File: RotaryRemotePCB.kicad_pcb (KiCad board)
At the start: 2 copper layers, 82 x 82 mm, 10 parts, among them J1 Conn_01x02, J2 UART, J3 i2c, J4 Neopixel Connector, J5 EncoderRotary, J6 EncoderSwitch, SW1 RotaryEncoder_Switch, U1 TP4056, U2 WeMos_D1_mini

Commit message: Add git submodule
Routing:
- net Net-(U1-Pad6): track 0.00 -> 5.75 mm
- net Net-(U1-Pad5): track 0.00 -> 5.15 mm

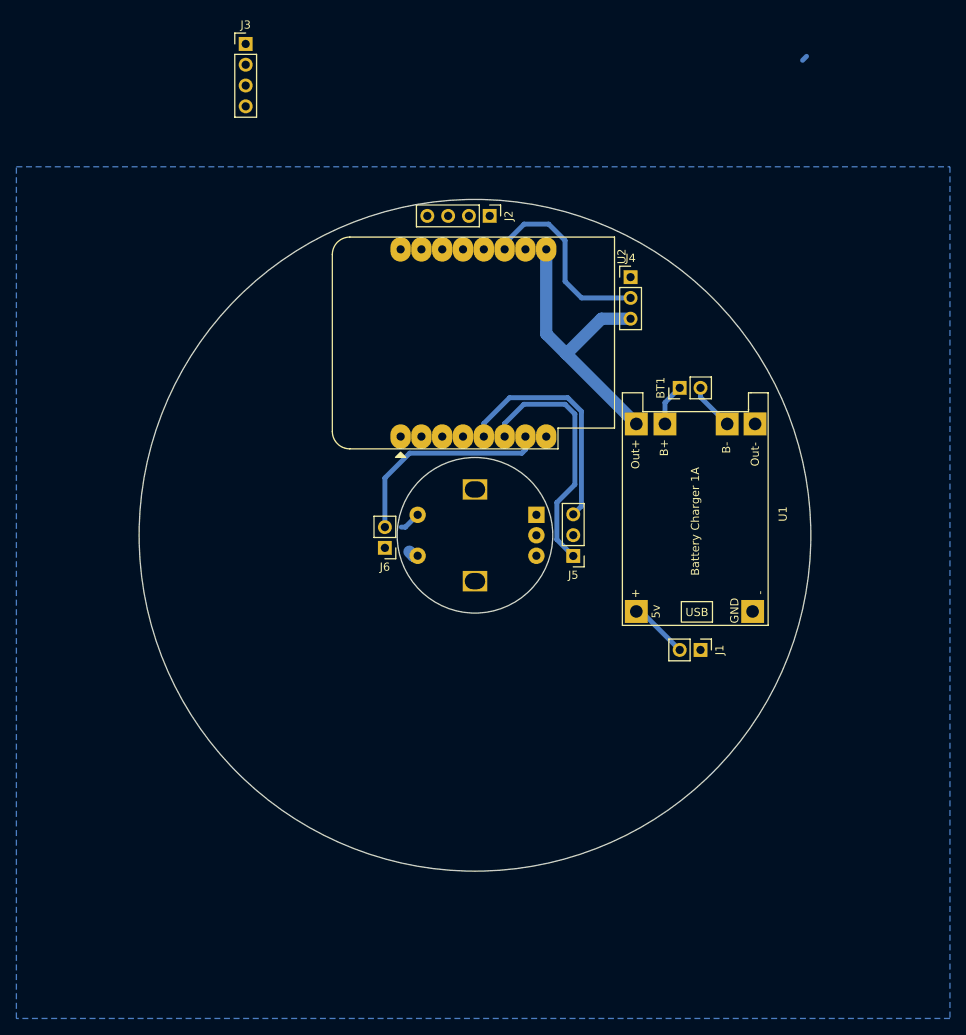
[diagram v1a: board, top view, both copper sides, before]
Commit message: Add FTDI connector
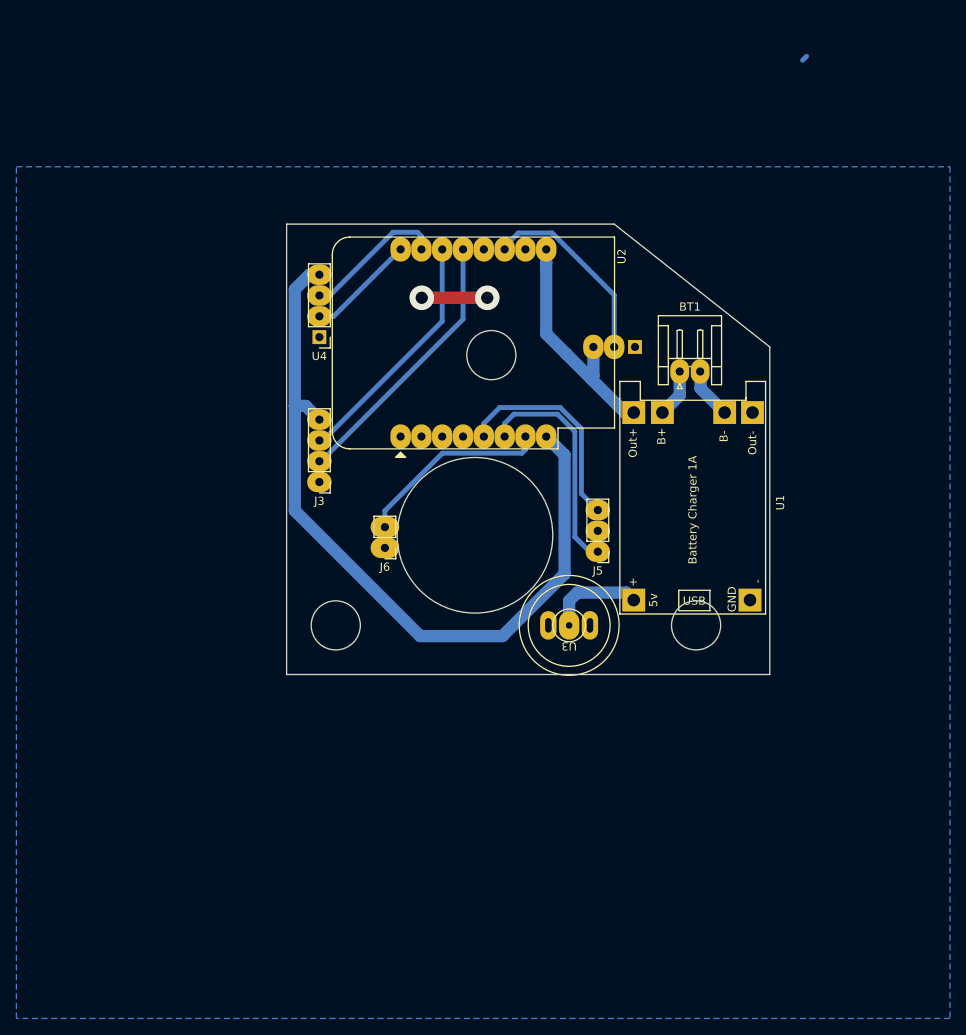
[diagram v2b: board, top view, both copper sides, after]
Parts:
- removed J1: Conn_01x02, Connector_PinHeader_2.54mm:PinHeader_1x02_P2.54mm_Vertical
- removed J2: UART, Connector_PinHeader_2.54mm:PinHeader_1x04_P2.54mm_Vertical
- removed SW1: RotaryEncoder_Switch, Rotary_Encoder:RotaryEncoder_Alps_EC12E-Switch_Vertical_H20mm
- added U3: magnetic-charger, magnetic-charger:magnetic-charger, F.Cu at (111.5, 111.0)
- added U4: TTL, Connector_PinHeader_2.54mm:PinHeader_1x04_P2.54mm_Vertical, F.Cu at (81.0, 75.8)
- BT1: footprint Connector_PinHeader_2.54mm:PinHeader_1x02_P2.54mm_Vertical -> Connector_JST:JST_EH_S2B-EH_1x02_P2.50mm_Horizontal
- J4: footprint Connector_PinHeader_2.54mm:PinHeader_1x03_P2.54mm_Vertical -> Connector_PinHeader_2.54mm:PinHeader_1x03_P2.54mm_Horizontal; moved to B.Cu
- moved J3 54.3 mm to (81.0, 93.5), turned to 180 degrees
- moved J4 8.54 mm to (119.5, 77.0), turned to 90 degrees
- moved J5 3.05 mm to (115.0, 102.0)
- moved BT1 2.00 mm to (125.0, 80.0), turned to 0 degrees
- moved U1 1.42 mm to (117.7, 109.6)
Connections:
- net Net-(U1-Pad5) renamed /VBAT
- net Net-(U1-Pad6) renamed /VBAT-
- J3 pad 1: unconnected-(J3-Pad1) -> GND
- J3 pad 2: unconnected-(J3-Pad2) -> SDA
- J3 pad 3: unconnected-(J3-Pad3) -> SCL
- J3 pad 4: unconnected-(J3-Pad4) -> +3V3
- U1 pad 1: Net-(J1-Pad2) -> /VIN
- U2 pad 13: unconnected-(U2-Pad13) -> SDA
- U2 pad 14: unconnected-(U2-Pad14) -> SCL
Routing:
- net +3V3: track 0.00 -> 94.6 mm
- net SDA: track 0.00 -> 34.3 mm
- net SCL: track 0.00 -> 30.8 mm
- net Net-(U2-Pad15): track 0.00 -> 17.5 mm
- net Net-(U2-Pad16): track 0.00 -> 13.3 mm
- net /VIN: track 0.00 -> 11.7 mm
- net Net-(J1-Pad2): track 7.25 -> 0.00 mm
- net GND: track 1.21 -> 8.00 mm, vias 0 -> 2
- net +5V: track 35.5 -> 29.0 mm
- net ROTARY_SWITCH: track 28.8 -> 23.8 mm
- net Net-(J5-Pad1): track 30.7 -> 28.0 mm
- net Net-(J5-Pad3): track 28.8 -> 26.2 mm
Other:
- board size 82 x 82 mm -> 59 x 55 mm

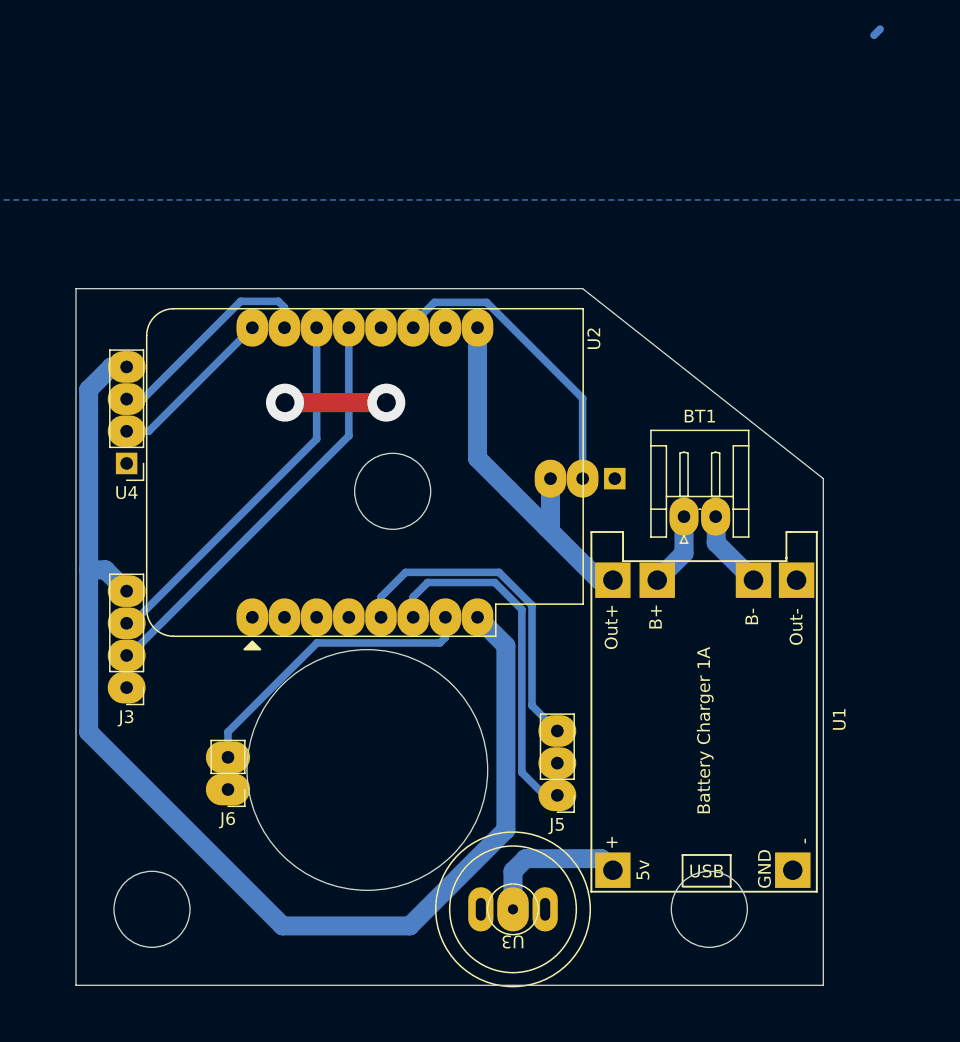
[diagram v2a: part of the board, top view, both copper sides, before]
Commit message: Update I2C Bus
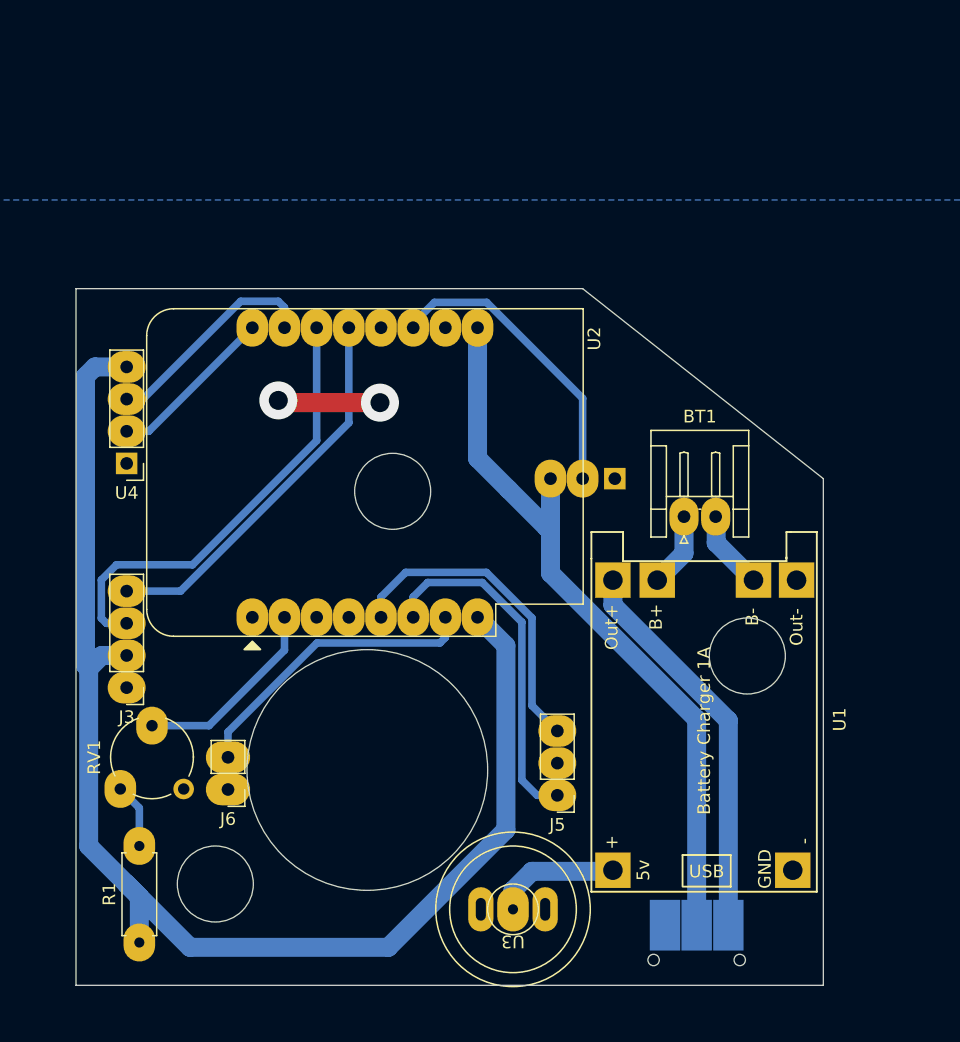
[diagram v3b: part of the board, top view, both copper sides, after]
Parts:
- added R1: 20k, Resistor_THT:R_Axial_DIN0207_L6.3mm_D2.5mm_P7.62mm_Horizontal, F.Cu at (82.0, 113.6)
- added RV1: 10k, Potentiometer_THT:Potentiometer_Piher_PT-6-V_Vertical, F.Cu at (85.5, 101.5)
- added SW2: SW_SPST, Button_Switch_SMD:SW_SPDT_CK-JS102011SAQN, B.Cu at (126.0, 115.0)
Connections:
- J3 pad 2: SDA -> +3V3
- J3 pad 4: +3V3 -> SDA
- U1 pad 3: +5V -> /5V
- U2 pad 2: unconnected-(U2-Pad2) -> Net-(U2-Pad2)
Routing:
- net /5V: track 0.00 -> 31.0 mm
- net +5V: track 29.0 -> 59.6 mm
- net Net-(U2-Pad2): track 0.00 -> 15.5 mm
- net +3V3: track 94.6 -> 108.2 mm
- net SCL: track 30.8 -> 37.1 mm
- net Net-(R1-Pad2): track 0.00 -> 5.12 mm
- net SDA: track 34.3 -> 30.6 mm
- net /VIN: track 11.7 -> 10.0 mm
- net (no net): track 0.69 -> 0.00 mm
- net Net-(J5-Pad3): track 26.2 -> 25.6 mm
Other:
- outline, holes or cut-outs redrawn
